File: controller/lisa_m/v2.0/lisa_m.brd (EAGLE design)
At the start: 50.7 x 33.6 mm, 119 parts, among them IC9 LP2992 5V, J1 CONN_3-1, J2 CONN_3-1, J3 CONN_3-1, J4 CONN_3-1, J5 CONN_3-1, J6 CONN_3-1, J7 CONN_3-1, J8 CONN_3-1, Q1 12Mhz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

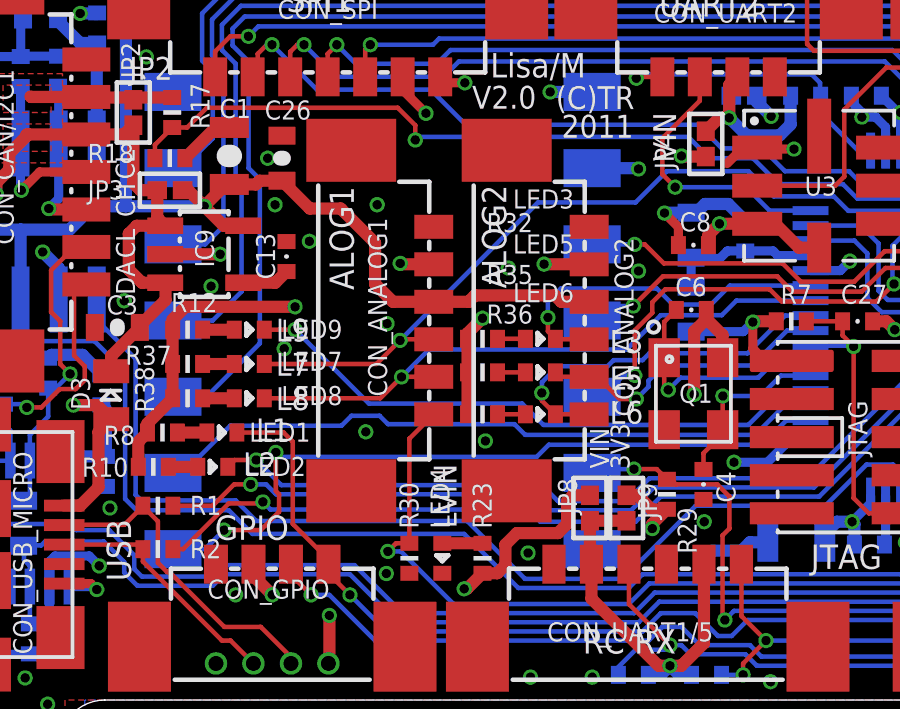
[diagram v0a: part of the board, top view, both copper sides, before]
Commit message: - switched analog1 and analog2 connector labels on schematic and silkscreen  - changed LED labels on schematic to be more intuitive and match software defines  - changed power led to LEDVIN from LED4 (can't be controlled) in schematic  - changed LED silkscreen label numbers to match new schematic labels
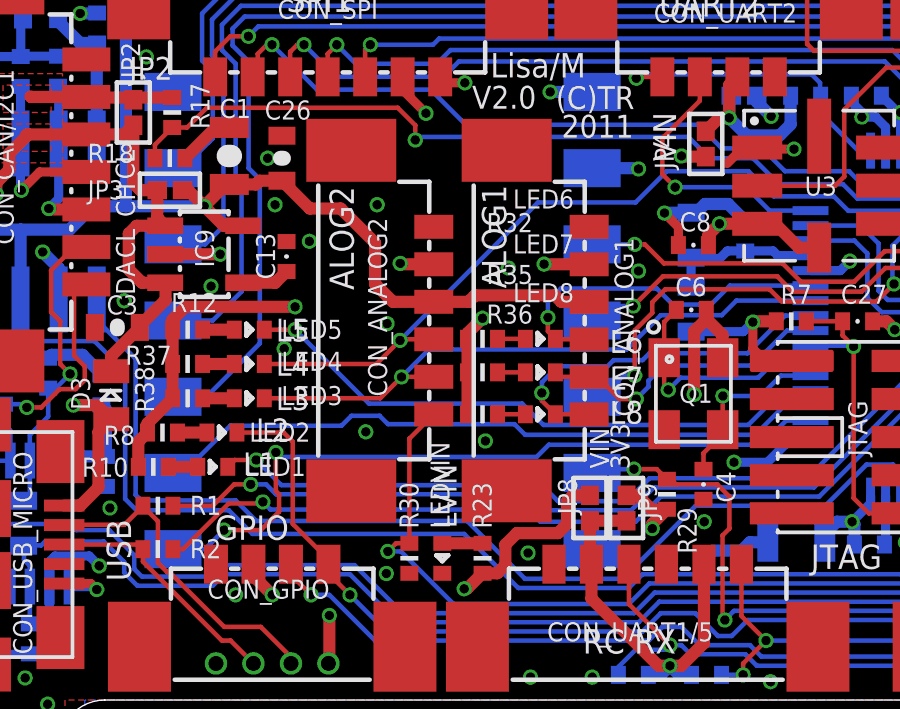
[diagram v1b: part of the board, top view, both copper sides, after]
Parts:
- removed LED9: GRN, pel_dipol_comp:0402-LED
- added LEDVIN: GRN, pel_dipol_comp:0402-LED
- LED1, LED4: value GRN -> RED
- LED2: value RED -> GRN
- LED3, LED5: value BLU -> GRN
- LED7: value RED -> BLU
- LED8: value GRN -> BLU
- moved LED3 9.90 mm to (10.5, 10.1)
- moved LED5 9.81 mm to (10.5, 12.3)
- moved LED8 9.72 mm to (20.2, 9.53)
- moved LED7 9.71 mm to (20.2, 10.9)
- moved LED4 9.13 mm to (10.5, 11.2), turned to 0 degrees
- moved CON_ANALOG1 5.18 mm to (20.6, 12.6)
- moved CON_ANALOG2 5.18 mm to (15.4, 12.6)
- moved LED6 2.51 mm to (20.2, 12.0)
- moved LED1 1.18 mm to (9.30, 7.77)
- moved LED2 1.18 mm to (9.60, 8.92)
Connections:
- net ADC_1: now also CON_ANALOG1.4, LED6.C; no longer CON_ANALOG2.4, LED3.C
- net ADC_2: now also CON_ANALOG1.5, LED7.C; no longer CON_ANALOG2.5, LED5.C
- net ADC_3: now also CON_ANALOG1.6, LED8.C; no longer CON_ANALOG2.6, LED6.C
- net ADC_4: now also CON_ANALOG2.4, LED4.C; no longer CON_ANALOG1.4, LED7.C
- net ADC_6: now also CON_ANALOG2.5, LED3.C; no longer CON_ANALOG1.5, LED8.C
- net BOOT0: now also CON_ANALOG2.6; no longer CON_ANALOG1.6
- net GND: now also LEDVIN.C; no longer LED4.C
- net JTAG_TRST: now also LED2.C; no longer LED1.C
- net LED1: now also LED1.C; no longer LED2.C
- net LED2: now also LED5.C; no longer LED9.C
- net N$10: now also LED2.A; no longer LED1.A
- net N$11: now also LED8.A; no longer LED6.A
- net N$12: now also LEDVIN.A; no longer LED4.A
- net N$13: now also LED5.A; no longer LED9.A
- net N$14: now also LED4.A; no longer LED7.A
- net N$15: now also LED3.A; no longer LED8.A
- net N$4: now also LED1.A; no longer LED2.A
- net N$5: now also LED6.A; no longer LED3.A
- net N$9: now also LED7.A; no longer LED5.A
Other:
- board text added: "L4"
- board text removed: "L9"
